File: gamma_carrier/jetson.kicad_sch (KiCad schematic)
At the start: 0 parts

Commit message: imported jetson som footprint successfully
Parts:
- added J1: Bus_DDR4_SODIMM_CUSTOM_Jetson-Orin-H9.2mm-socket, gamma_fp:TE_2309413, symbol antmicroSoMConnectors:Bus_DDR4_SODIMM_CUSTOM_Jetson-Orin-H9.2mm-socket
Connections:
- new net GND: J1.1 (GND), J1.102 (GND), J1.107 (GND), J1.113 (GND), J1.119 (GND), J1.125 (GND), J1.129 (GND), J1.13 (GND), J1.132 (GND), J1.135 (GND), J1.138 (GND), J1.14 (GND), J1.141 (GND), J1.144 (GND), J1.146 (GND), J1.147 (GND), J1.152 (GND), J1.153 (GND), J1.158 (GND), J1.159 (GND), J1.164 (GND), J1.165 (GND), J1.170 (GND), J1.171 (GND), J1.176 (GND), J1.177 (GND), J1.19 (GND), J1.2 (GND), J1.20 (GND), J1.200 (GND), J1.201 (GND), J1.231 (GND), J1.241 (GND), J1.242 (GND), J1.243 (GND), J1.244 (GND), J1.245 (GND), J1.246 (GND), J1.247 (GND), J1.248 (GND), J1.249 (GND), J1.25 (GND), J1.250 (GND), J1.26 (GND), J1.31 (GND), J1.32 (GND), J1.37 (GND), J1.38 (GND), J1.43 (GND), J1.44 (GND), J1.49 (GND), J1.50 (GND), J1.55 (GND), J1.56 (GND), J1.61 (GND), J1.62 (GND), J1.67 (GND), J1.68 (GND), J1.7 (GND), J1.73 (GND), J1.74 (GND), J1.79 (GND), J1.8 (GND), J1.80 (GND), J1.85 (GND), J1.86 (GND)
- new net VDD_5V: J1.251 (VDD_IN), J1.252 (VDD_IN), J1.253 (VDD_IN), J1.254 (VDD_IN), J1.255 (VDD_IN), J1.256 (VDD_IN), J1.257 (VDD_IN), J1.258 (VDD_IN), J1.259 (VDD_IN), J1.260 (VDD_IN)

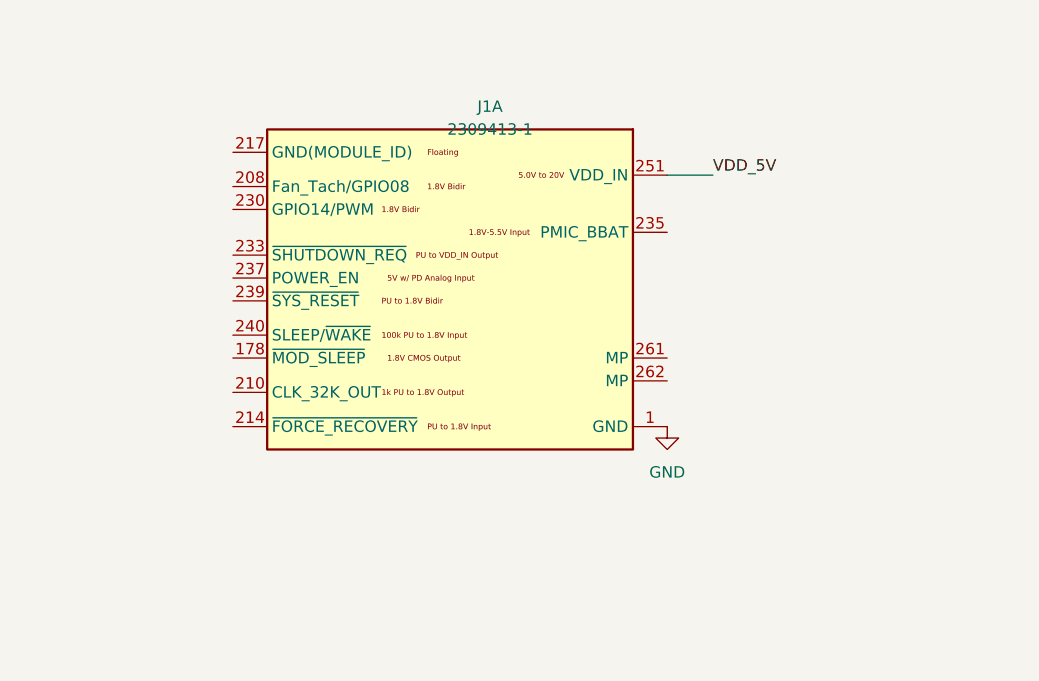
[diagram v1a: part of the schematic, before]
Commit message: jetson power done, need fan and revision
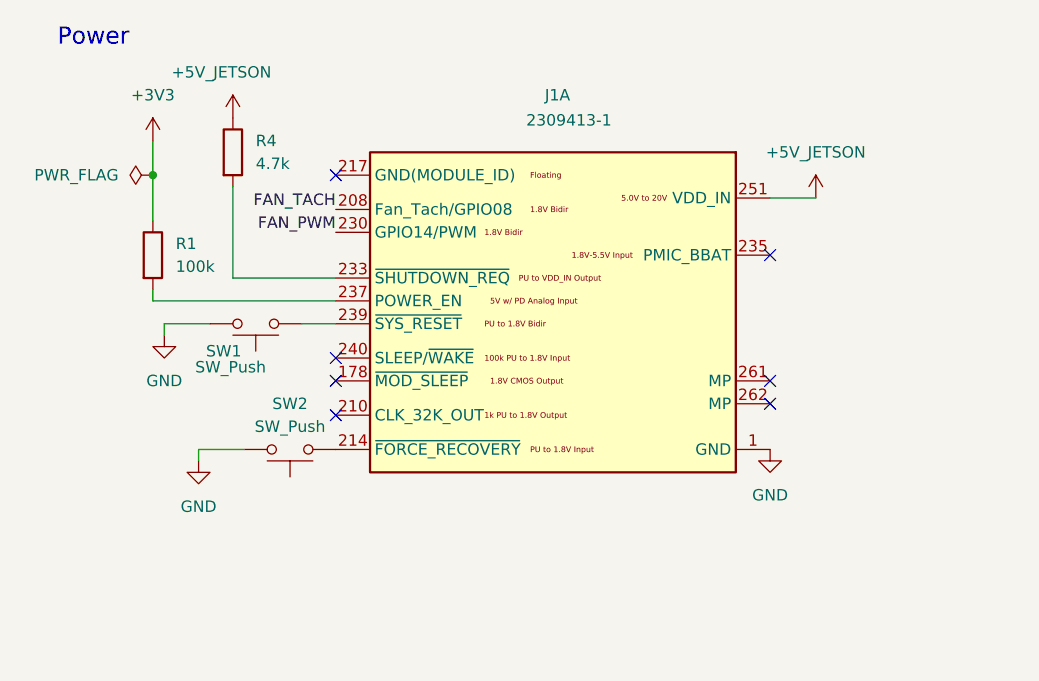
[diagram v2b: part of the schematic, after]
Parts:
- added R1: 100k, symbol Device:R
- added R4: 4.7k, symbol Device:R
- added SW1, SW2: SW_Push, symbol Switch:SW_Push
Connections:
- net GND: now also SW1.1, SW2.1
- net FAN_TACH: now reaches J1.208 (Fan_Tach/GPIO08)
- net at J1.214 (~{FORCE_RECOVERY}): now also SW2.2
- net FAN_PWM: now reaches J1.230 (GPIO14/PWM)
- net at J1.233 (~{SHUTDOWN_REQ}): now also R4.2
- net at J1.237 (POWER_EN): now also R1.2
- net at J1.239 (~{SYS_RESET}): now also SW1.2
- net VDD_5V renamed +5V_JETSON
- net +5V_JETSON: now also R4.1
- new net +3V3: R1.1
- no-connect marks 0 -> 7
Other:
- note added: "Power"
- moved on the sheet: J1A
